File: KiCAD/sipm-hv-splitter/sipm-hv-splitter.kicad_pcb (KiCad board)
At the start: 2 copper layers, 139.7 x 33 mm, 120 parts, among them J1 Conn_02x18_Odd_Even, J2 Conn_02x17_Odd_Even, Q1 BSS138, Q2 BSS138, Q3 BSS138, U1 ATmega328-M, U10 OPA810xDCK, U11 OPA810xDCK, U12 OPA810xDCK, U13 OPA810xDCK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

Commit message: starting placement
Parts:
- added C48: 1.0uF, Capacitor_SMD:C_0603_1608Metric_Pad1.08x0.95mm_HandSolder, F.Cu at (109.0, 92.8)
- added C49: 2.2uF, Capacitor_SMD:C_0603_1608Metric_Pad1.08x0.95mm_HandSolder, F.Cu at (109.0, 95.3)
- added C50: 1.0uF, Capacitor_SMD:C_0603_1608Metric_Pad1.08x0.95mm_HandSolder, F.Cu at (109.0, 97.8)
- added C51: 2.2uF, Capacitor_SMD:C_0603_1608Metric_Pad1.08x0.95mm_HandSolder, F.Cu at (109.0, 100.3)
- added U14: TPS7A25, Package_SON:WSON-6-1EP_2x2mm_P0.65mm_EP1x1.6mm_ThermalVias, F.Cu at (103.3, 94.8)
- added U16: TPS7A25, Package_SON:WSON-6-1EP_2x2mm_P0.65mm_EP1x1.6mm_ThermalVias, F.Cu at (103.3, 98.4)
- C4: value 12nF -> 0.1uF
- C9: value 3.3uF 100V -> 4.7uF 100V
- R13: value R_US -> 150k
- R14: value R_US -> 2.49k
- R6: value 9.76k -> 10k
- moved R37 132.8 mm to (176.5, 55.2)
- moved R29 127.1 mm to (168.7, 53.5), turned to 180 degrees
- moved C40 125.8 mm to (176.5, 57.1)
- moved R21 125.0 mm to (172.7, 57.1), turned to 180 degrees
- moved C32 122.8 mm to (172.7, 55.2), turned to 180 degrees
- moved C16 120.4 mm to (172.7, 53.5)
- moved C24 115.9 mm to (168.6, 58.3)
- moved U6 113.3 mm to (168.6, 55.9)
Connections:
- C16 pad 1: +3.3V -> +3.3VA
- C17 pad 1: +3.3V -> +3.3VA
- C18 pad 1: +3.3V -> +3.3VA
- C19 pad 1: +3.3V -> +3.3VA
- C20 pad 1: +3.3V -> +3.3VA
- C21 pad 1: +3.3V -> +3.3VA
- C22 pad 1: +3.3V -> +3.3VA
- C23 pad 1: +3.3V -> +3.3VA
- J2 pad 10: /-20V -> -24V
- J2 pad 14: /-20V -> -24V
- J2 pad 18: /-20V -> -24V
- J2 pad 2: /-20V -> -24V
- J2 pad 22: /-20V -> -24V
- J2 pad 26: /-20V -> -24V
- J2 pad 30: /-20V -> -24V
- J2 pad 6: /-20V -> -24V
- U10 pad 5: +3.3V -> +3.3VA
- U11 pad 5: +3.3V -> +3.3VA
- U12 pad 5: +3.3V -> +3.3VA
- U13 pad 5: +3.3V -> +3.3VA
- U6 pad 5: +3.3V -> +3.3VA
- U7 pad 5: +3.3V -> +3.3VA
- U8 pad 5: +3.3V -> +3.3VA
- U9 pad 5: +3.3V -> +3.3VA

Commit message: random placement for area estimate
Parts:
- moved R38 95.2 mm to (120.5, 62.8)
- moved R42 94.6 mm to (108.1, 62.7)
- moved R30 90.7 mm to (112.7, 61.0), turned to 180 degrees
- moved R34 90.1 mm to (100.2, 60.9), turned to 180 degrees
- moved C41 87.4 mm to (120.5, 64.7)
- moved R22 87.3 mm to (116.7, 64.7), turned to 180 degrees
- moved R26 86.7 mm to (104.2, 64.6), turned to 180 degrees
- moved C45 86.7 mm to (108.1, 64.6)
- moved C33 84.7 mm to (116.7, 62.8), turned to 180 degrees
- moved C37 84.0 mm to (104.2, 62.7), turned to 180 degrees
- moved R41 82.8 mm to (108.1, 54.9)
- moved C17 82.1 mm to (116.7, 61.0)
- moved C21 81.3 mm to (104.3, 60.9)
- moved R33 80.6 mm to (100.2, 53.1), turned to 180 degrees
- moved C25 77.8 mm to (112.6, 65.9)
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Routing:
- net GND: track 0.00 -> 28.5 mm, vias 0 -> 32
- net -24V: track 0.00 -> 27.7 mm
- net +3.3VA: track 0.00 -> 17.9 mm, vias 0 -> 16
- net Net-(U10--): track 0.00 -> 13.6 mm
- net Net-(U11--): track 0.00 -> 13.6 mm
- net Net-(U12--): track 0.00 -> 13.6 mm
- net Net-(U8--): track 0.00 -> 13.6 mm
- net Net-(U7--): track 0.00 -> 13.6 mm
- net Net-(U13--): track 0.00 -> 13.6 mm
- net Net-(U9--): track 0.00 -> 13.6 mm
- net Net-(U6--): track 0.00 -> 13.6 mm
- net Net-(C38-Pad2): track 0.00 -> 7.83 mm
- net Net-(C35-Pad2): track 0.00 -> 7.83 mm
- net Net-(C32-Pad2): track 0.00 -> 7.83 mm
- net Net-(C33-Pad2): track 0.00 -> 7.83 mm
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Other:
- board size 139.7 x 33 mm -> 82.5 x 33 mm
- copper layers 2 -> 6

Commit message: add ISP
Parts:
- added C52: 1.0uF, Capacitor_SMD:C_0603_1608Metric_Pad1.08x0.95mm_HandSolder, F.Cu at (78.7, 72.4)
- added J3: -OMIT-, Connector_PinHeader_1.00mm:PinHeader_1x06_P1.00mm_Vertical, F.Cu at (91.5, 82.5)
- added R45: 4.7k, Resistor_SMD:R_0603_1608Metric_Pad0.98x0.95mm_HandSolder, F.Cu at (83.8, 82.5)
- C10: footprint Capacitor_SMD:C_0603_1608Metric_Pad1.08x0.95mm_HandSolder -> Capacitor_SMD:C_1206_3216Metric_Pad1.33x1.80mm_HandSolder
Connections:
- C48 pad 2: Net-(U16-GND) -> GND
- C49 pad 2: Net-(U16-GND) -> GND
- C50 pad 2: Net-(U14-GND) -> GND
- C51 pad 2: Net-(U14-GND) -> GND
- U1 pad 18: unconnected-(U1-AVCC-Pad18) -> +3.3V
- U1 pad 21: Net-(U1-GND-Pad21) -> GND
- U1 pad 3: Net-(U1-GND-Pad21) -> GND
- U1 pad 30: unconnected-(U1-PD0-Pad30) -> /COMM/RX
- U1 pad 31: unconnected-(U1-PD1-Pad31) -> /COMM/TX
- U1 pad 33: Net-(U1-GND-Pad21) -> GND
- U1 pad 4: Net-(U1-VCC-Pad4) -> +3.3V
- U1 pad 5: Net-(U1-GND-Pad21) -> GND
- U1 pad 6: Net-(U1-VCC-Pad4) -> +3.3V
- U14 pad 5: Net-(U14-GND) -> GND
- U14 pad 7: Net-(U14-GND) -> GND
- U16 pad 5: Net-(U16-GND) -> GND
- U16 pad 7: Net-(U16-GND) -> GND

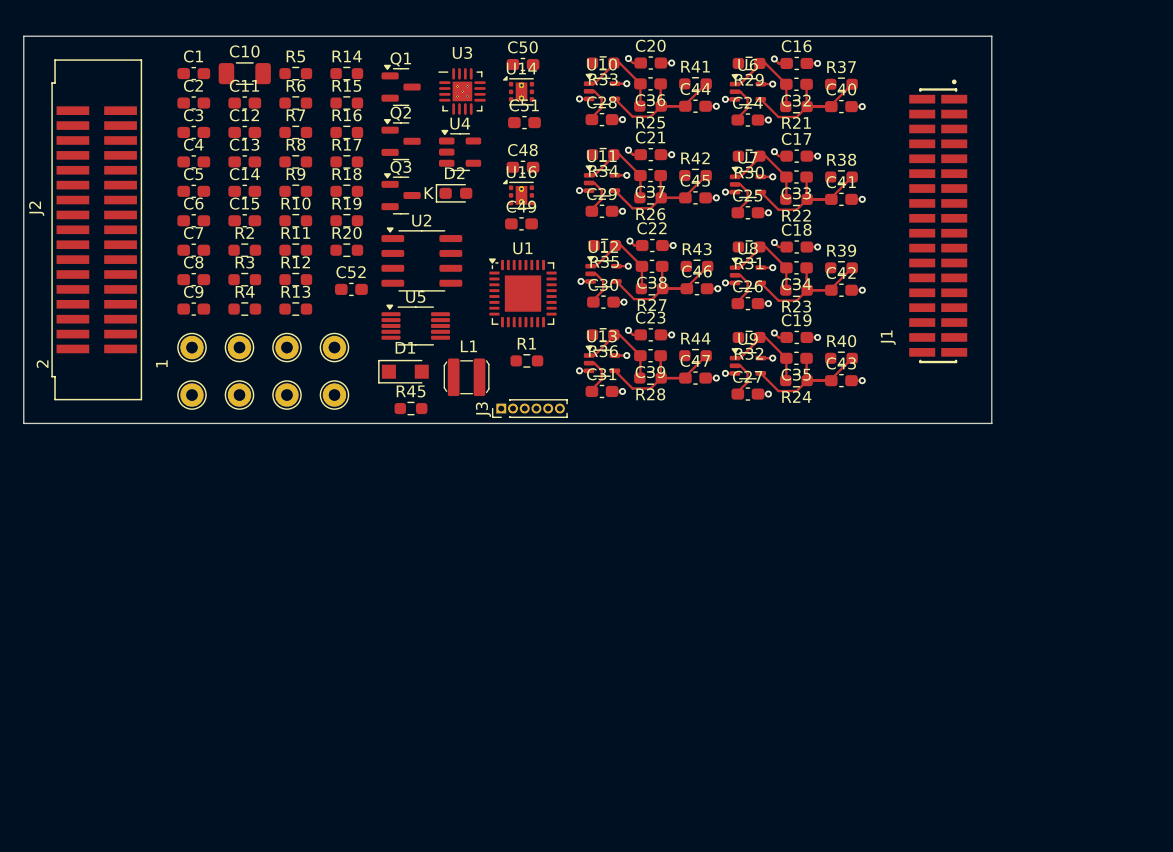
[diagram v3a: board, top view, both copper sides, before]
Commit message: working on 2.5 in placement
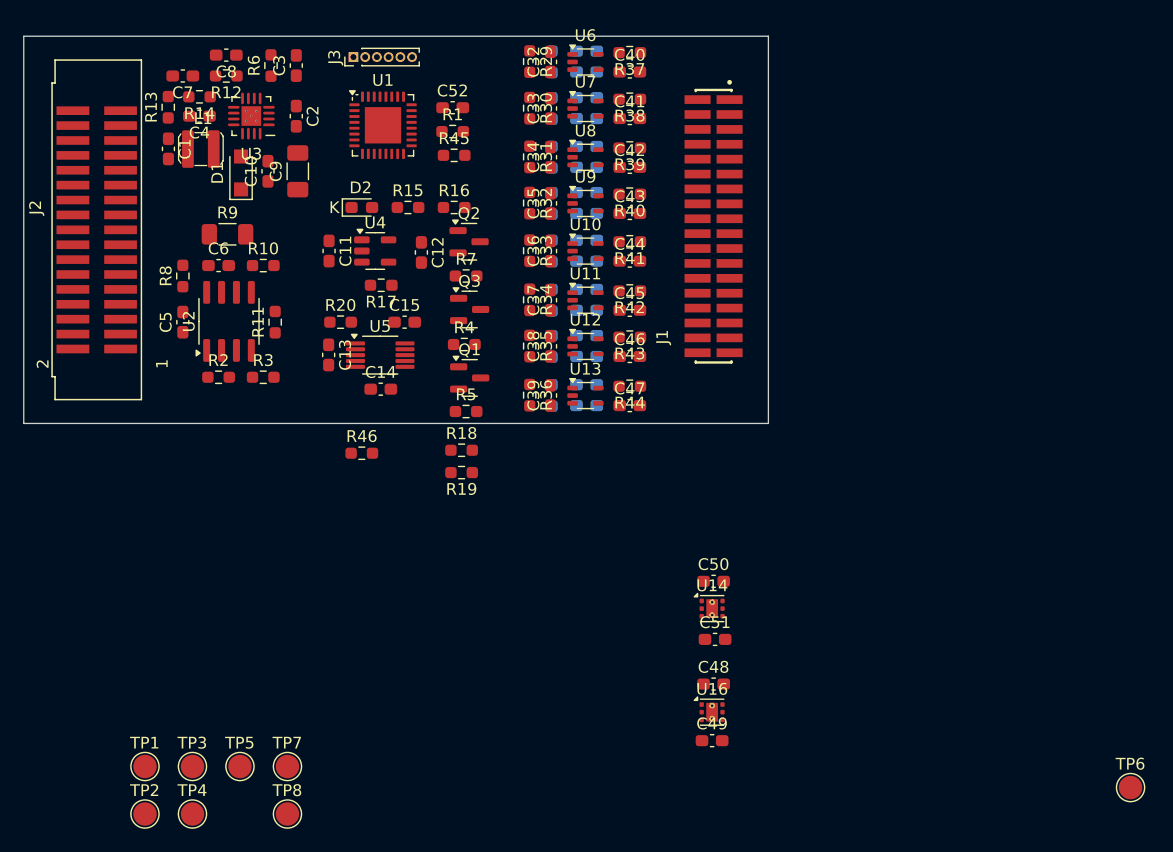
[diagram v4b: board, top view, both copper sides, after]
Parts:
- added R46: 10.0k, Resistor_SMD:R_0603_1608Metric_Pad0.98x0.95mm_HandSolder, F.Cu at (79.6, 86.4)
- C10: footprint Capacitor_SMD:C_1206_3216Metric_Pad1.33x1.80mm_HandSolder -> Capacitor_SMD:C_0603_1608Metric_Pad1.08x0.95mm_HandSolder
- C16, C17, C18, C19, C20, C21, C22, C23, C24, C25, C26, C27, C28, C29, C30, C31, R21, R22, R23, R24, R25, R26, R27, R28: moved to B.Cu
- C9: footprint Capacitor_SMD:C_0603_1608Metric_Pad1.08x0.95mm_HandSolder -> Capacitor_SMD:C_1206_3216Metric_Pad1.33x1.80mm_HandSolder
- R9: footprint Resistor_SMD:R_0603_1608Metric_Pad0.98x0.95mm_HandSolder -> Resistor_SMD:R_1206_3216Metric_Pad1.30x1.75mm_HandSolder
- TP1, TP2, TP3, TP4, TP5, TP6, TP7, TP8: footprint my_tp:tp_SMT_label2 -> TestPoint:TestPoint_Pad_D2.0mm
- moved TP6 79.3 mm to (145.2, 114.9)
- moved C48 47.0 mm to (109.6, 106.0)
- moved U14 47.0 mm to (109.5, 99.6)
- moved U16 47.0 mm to (109.5, 108.4)
- moved C50 47.0 mm to (109.6, 97.3)
- moved C51 47.0 mm to (109.8, 102.2)
- moved C49 47.0 mm to (109.5, 110.9)
- moved TP2 36.0 mm to (61.1, 117.1)
- moved TP4 36.0 mm to (65.2, 117.1)
- moved TP8 36.0 mm to (73.3, 117.1)
- moved TP1 36.0 mm to (61.1, 113.1)
- moved TP3 36.0 mm to (65.2, 113.1)
- moved TP5 36.0 mm to (69.2, 113.1)
- moved TP7 36.0 mm to (73.3, 113.1)
- moved J3 32.5 mm to (78.9, 52.6)
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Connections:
- C3 pad 1: Net-(U3-BIAS) -> +12V
- J1 pad 4: /TEMP -> /THERM
- U1 pad 10: /ADC_IMON -> unconnected-(U1-PD6-Pad10)
- U1 pad 11: /ADC_VMON -> unconnected-(U1-PD7-Pad11)
- U1 pad 23: unconnected-(U1-PC0-Pad23) -> /ADC_IMON
- U1 pad 24: unconnected-(U1-PC1-Pad24) -> /ADC_VMON
- U1 pad 25: unconnected-(U1-PC2-Pad25) -> /THERM
- U3 pad 3: Net-(U3-BIAS) -> +12V
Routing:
- net GND: track 28.5 -> 0.00 mm, vias 32 -> 0
- net -24V: track 27.7 -> 0.00 mm
- net +3.3VA: track 17.9 -> 0.00 mm, vias 16 -> 0
- net Net-(U10--): track 13.6 -> 0.00 mm
- net Net-(U11--): track 13.6 -> 0.00 mm
- net Net-(U12--): track 13.6 -> 0.00 mm
- net Net-(U8--): track 13.6 -> 0.00 mm
- net Net-(U7--): track 13.6 -> 0.00 mm
- net Net-(U13--): track 13.6 -> 0.00 mm
- net Net-(U9--): track 13.6 -> 0.00 mm
- net Net-(U6--): track 13.6 -> 0.00 mm
- net Net-(C38-Pad2): track 7.83 -> 0.00 mm
- net Net-(C35-Pad2): track 7.83 -> 0.00 mm
- net Net-(C32-Pad2): track 7.83 -> 0.00 mm
- net Net-(C33-Pad2): track 7.83 -> 0.00 mm
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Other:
- board size 82.5 x 33 mm -> 63.5 x 33 mm

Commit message: routing madness
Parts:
- added D3: LED, my_smt_led:my_SMT_0603, F.Cu at (85.5, 53.1)
- added R47: 1.5k, Resistor_SMD:R_0603_1608Metric_Pad0.98x0.95mm_HandSolder, F.Cu at (89.4, 53.1)
- TP1, TP2, TP3, TP4, TP5, TP6, TP7, TP8: footprint TestPoint:TestPoint_Pad_D2.0mm -> TestPoint:TestPoint_Pad_D1.0mm
- U1: footprint Package_DFN_QFN:QFN-32-1EP_5x5mm_P0.5mm_EP3.1x3.1mm -> my_QFN:QFN-32-1EP_5x5mm_P0.5mm_EP3.1x3.1mm
- U10, U11, U12, U13, U6, U7, U8, U9: footprint Package_TO_SOT_SMD:Texas_R-PDSO-G5_DCK-5 -> my_SC70:Texas_R-PDSO-G5_DCK-5
- moved TP6 80.4 mm to (77.9, 70.9)
- moved TP7 59.2 mm to (84.6, 55.0)
- moved TP4 51.4 mm to (74.8, 66.7)
- moved TP2 50.6 mm to (65.0, 66.7)
- moved C51 50.2 mm to (63.9, 81.9), turned to 180 degrees
- moved TP8 47.8 mm to (84.8, 70.7)
- moved U14 45.8 mm to (67.3, 81.9)
- moved C49 45.4 mm to (74.5, 81.9), turned to 180 degrees
- moved TP3 42.3 mm to (72.9, 71.5)
- moved TP5 42.1 mm to (81.0, 72.6)
- moved C50 41.8 mm to (70.7, 81.9)
- moved U16 41.3 mm to (77.9, 81.9)
- moved C48 37.1 mm to (81.4, 81.9)
- moved TP1 34.1 mm to (64.8, 79.1)
- moved R46 32.3 mm to (87.5, 55.0)
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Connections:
- net /BOOST/+62V renamed /BOOST/62V
- net Net-(U4-VIN) renamed /BOOST/V62_IN
- J1 pad 1: /DET_0 -> /THERM
- J1 pad 10: /VBIAS -> /DET_5
- J1 pad 12: unconnected-(J1-Pin_12-Pad12) -> /VBIAS
- J1 pad 13: /DET_3 -> unconnected-(J1-Pin_13-Pad13)
- J1 pad 14: /VBIAS -> /DET_4
- J1 pad 16: unconnected-(J1-Pin_16-Pad16) -> /VBIAS
- J1 pad 17: /DET_4 -> unconnected-(J1-Pin_17-Pad17)
- J1 pad 18: /VBIAS -> /DET_3
- J1 pad 2: /VBIAS -> /DET_7
- J1 pad 20: unconnected-(J1-Pin_20-Pad20) -> /VBIAS
- J1 pad 21: /DET_5 -> unconnected-(J1-Pin_21-Pad21)
- J1 pad 22: /VBIAS -> /DET_2
- J1 pad 24: unconnected-(J1-Pin_24-Pad24) -> /VBIAS
- J1 pad 25: /DET_6 -> unconnected-(J1-Pin_25-Pad25)
- J1 pad 26: /VBIAS -> /DET_1
- J1 pad 28: unconnected-(J1-Pin_28-Pad28) -> /VBIAS
- J1 pad 29: /DET_7 -> unconnected-(J1-Pin_29-Pad29)
- J1 pad 30: /VBIAS -> /DET_0
- J1 pad 32: unconnected-(J1-Pin_32-Pad32) -> /VBIAS
- J1 pad 35: GND -> unconnected-(J1-Pin_35-Pad35)
- J1 pad 4: /THERM -> /VBIAS
- J1 pad 5: /DET_1 -> unconnected-(J1-Pin_5-Pad5)
- J1 pad 6: /VBIAS -> /DET_6
- J1 pad 8: unconnected-(J1-Pin_8-Pad8) -> /VBIAS
- J1 pad 9: /DET_2 -> unconnected-(J1-Pin_9-Pad9)
- R29 pad 2: /SIG_0 -> /SIG_7
- R30 pad 2: /SIG_1 -> /SIG_6
- R31 pad 2: /SIG_2 -> /SIG_5
- R32 pad 2: /SIG_3 -> /SIG_4
- R33 pad 2: /SIG_4 -> /SIG_3
- R34 pad 2: /SIG_5 -> /SIG_2
- R35 pad 2: /SIG_6 -> /SIG_1
- R36 pad 2: /SIG_7 -> /SIG_0
- R37 pad 1: /DET_0 -> /DET_7
- R38 pad 1: /DET_1 -> /DET_6
- R39 pad 1: /DET_2 -> /DET_5
- R40 pad 1: /DET_3 -> /DET_4
- R41 pad 1: /DET_4 -> /DET_3
- R42 pad 1: /DET_5 -> /DET_2
- R43 pad 1: /DET_6 -> /DET_1
- R44 pad 1: /DET_7 -> /DET_0
- U1 pad 32: unconnected-(U1-PD2-Pad32) -> Net-(U1-PD2)
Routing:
- net GND: track 0.00 -> 81.5 mm, vias 0 -> 65
- net /SIG_7: track 0.00 -> 45.2 mm, vias 0 -> 2
- net /SIG_6: track 0.00 -> 43.7 mm, vias 0 -> 2
- net /SIG_5: track 0.00 -> 43.4 mm, vias 0 -> 2
- net /SIG_4: track 0.00 -> 42.4 mm, vias 0 -> 2
- net /MISO: track 0.00 -> 36.7 mm, vias 0 -> 2
- net /COMM/RX: track 0.00 -> 30.8 mm, vias 0 -> 2
- net /COMM/TX: track 0.00 -> 26.0 mm, vias 0 -> 2
- net /VR_SHDN: track 0.00 -> 24.8 mm, vias 0 -> 2
- net +12V: track 0.00 -> 24.3 mm, vias 0 -> 19
- net -24V: track 0.00 -> 22.6 mm, vias 0 -> 10
- net +3.3VA: track 0.00 -> 21.1 mm, vias 0 -> 8
- net /~{RESET}: track 0.00 -> 18.7 mm, vias 0 -> 1
- net /BOOST_ENA: track 0.00 -> 18.7 mm, vias 0 -> 2
- net /MOSI: track 0.00 -> 18.7 mm
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- added copper zone on In4.Cu, net +12V
- added copper zone on In4.Cu, net +3.3V
- added copper zone on In3.Cu, net +3.3VA
- added copper zone on In3.Cu, net -24V
- added copper zone on F.Cu, net /BOOST/62V
- added copper zone on F.Cu, net /BOOST/V62_IN
- added copper zone on In4.Cu, net /VBIAS
- added copper zone on In1.Cu, net GND
- added copper zone on F.Cu, net Net-(D1-A)

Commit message: working on bias filter changes
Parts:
- added C53: 1.0uF, Capacitor_SMD:C_0603_1608Metric_Pad1.08x0.95mm_HandSolder, F.Cu at (82.0, 49.1)
- C40, R37: moved to B.Cu
- R21, R22, R23, R24, R25, R26, R27, R28: value 4.7k -> 15k
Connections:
- C32 pad 1: Net-(U6--) -> /DET_7
- C33 pad 1: Net-(U7--) -> /DET_6
- C34 pad 1: Net-(U8--) -> /DET_5
- C35 pad 1: Net-(U9--) -> /DET_4
- C36 pad 1: Net-(U10--) -> /DET_3
- C37 pad 1: Net-(U11--) -> /DET_2
- C38 pad 1: Net-(U12--) -> /DET_1
- C39 pad 1: Net-(U13--) -> /DET_0
- C40 pad 1: Net-(U6--) -> /TIA_0/SIPM_K
- C41 pad 1: Net-(U7--) -> /TIA_1/SIPM_K
- C42 pad 1: Net-(U8--) -> /TIA_2/SIPM_K
- C43 pad 1: Net-(U9--) -> /TIA_3/SIPM_K
- C44 pad 1: Net-(U10--) -> /TIA_4/SIPM_K
- C45 pad 1: Net-(U11--) -> /TIA_5/SIPM_K
- C46 pad 1: Net-(U12--) -> /TIA_6/SIPM_K
- C47 pad 1: Net-(U13--) -> /TIA_7/SIPM_K
- J1 pad 12: /VBIAS -> /TIA_2/SIPM_K
- J1 pad 16: /VBIAS -> /TIA_3/SIPM_K
- J1 pad 20: /VBIAS -> /TIA_4/SIPM_K
- J1 pad 24: /VBIAS -> /TIA_5/SIPM_K
- J1 pad 28: /VBIAS -> unconnected-(J1-Pin_28-Pad28)
- J1 pad 32: /VBIAS -> /TIA_7/SIPM_K
- J1 pad 4: /VBIAS -> /TIA_0/SIPM_K
- J1 pad 8: /VBIAS -> /TIA_1/SIPM_K
- J2 pad 33: /COMM/TX -> /COMM/RX
- J2 pad 34: /COMM/RX -> /COMM/TX
- R1 pad 1: /COMM/TX -> /COMM/RX
- R1 pad 2: /COMM/RX -> /COMM/TX
- R21 pad 1: Net-(U6--) -> /DET_7
- R22 pad 1: Net-(U7--) -> /DET_6
- R23 pad 1: Net-(U8--) -> /DET_5
- R24 pad 1: Net-(U9--) -> /DET_4
- R25 pad 1: Net-(U10--) -> /DET_3
- R26 pad 1: Net-(U11--) -> /DET_2
- R27 pad 1: Net-(U12--) -> /DET_1
- R28 pad 1: Net-(U13--) -> /DET_0
- R37 pad 1: /DET_7 -> /VBIAS
- R37 pad 2: Net-(U6--) -> /TIA_0/SIPM_K
- R38 pad 1: /DET_6 -> /VBIAS
- R38 pad 2: Net-(U7--) -> /TIA_1/SIPM_K
- R39 pad 1: /DET_5 -> /VBIAS
- R39 pad 2: Net-(U8--) -> /TIA_2/SIPM_K
- R40 pad 1: /DET_4 -> /VBIAS
- R40 pad 2: Net-(U9--) -> /TIA_3/SIPM_K
- R41 pad 1: /DET_3 -> /VBIAS
- R41 pad 2: Net-(U10--) -> /TIA_4/SIPM_K
- R42 pad 1: /DET_2 -> /VBIAS
- R42 pad 2: Net-(U11--) -> /TIA_5/SIPM_K
- R43 pad 1: /DET_1 -> /VBIAS
- R43 pad 2: Net-(U12--) -> /TIA_6/SIPM_K
- R44 pad 1: /DET_0 -> /VBIAS
- R44 pad 2: Net-(U13--) -> /TIA_7/SIPM_K
- U10 pad 4: Net-(U10--) -> /DET_3
- U11 pad 4: Net-(U11--) -> /DET_2
- U12 pad 4: Net-(U12--) -> /DET_1
- U13 pad 4: Net-(U13--) -> /DET_0
- U6 pad 4: Net-(U6--) -> /DET_7
- U7 pad 4: Net-(U7--) -> /DET_6
- U8 pad 4: Net-(U8--) -> /DET_5
- U9 pad 4: Net-(U9--) -> /DET_4
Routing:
- net Net-(U11--): track 9.40 -> 0.00 mm, vias 1 -> 0
- net /DET_2: track 0.00 -> 9.40 mm, vias 0 -> 1
- net Net-(U7--): track 9.40 -> 0.00 mm, vias 1 -> 0
- net Net-(U12--): track 9.40 -> 0.00 mm, vias 1 -> 0
- net Net-(U10--): track 9.40 -> 0.00 mm, vias 1 -> 0
- net /DET_3: track 0.00 -> 9.40 mm, vias 0 -> 1
- net /DET_1: track 0.00 -> 9.40 mm, vias 0 -> 1
- net Net-(U9--): track 9.40 -> 0.00 mm, vias 1 -> 0
- net /DET_4: track 0.00 -> 9.40 mm, vias 0 -> 1
- net Net-(U8--): track 9.40 -> 0.00 mm, vias 1 -> 0
- net Net-(U6--): track 9.40 -> 0.00 mm, vias 1 -> 0
- net /DET_5: track 0.00 -> 9.40 mm, vias 0 -> 1
- net Net-(U13--): track 8.77 -> 0.00 mm, vias 1 -> 0
- net /DET_0: track 0.00 -> 8.77 mm, vias 0 -> 1
- net /TIA_0/SIPM_K: track 0.00 -> 5.06 mm, vias 0 -> 1
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
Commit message: routing
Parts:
- C41, C42, C43, C44, C45, C46, C47, R38, R39, R40, R41, R42, R43, R44: moved to B.Cu
- moved C53 13.4 mm to (88.6, 60.8)
- moved R1 11.6 mm to (77.1, 53.8), turned to -90 degrees
- moved R46 4.22 mm to (88.6, 59.1)
- moved R45 3.86 mm to (88.6, 57.3)
- moved C8 3.37 mm to (71.0, 54.1)
- moved D3 3.20 mm to (88.6, 53.5), turned to 180 degrees
- moved J3 2.92 mm to (79.9, 53.2)
- moved R47 2.53 mm to (88.6, 55.5), turned to 0 degrees
- moved R6 1.74 mm to (73.5, 53.8)
- moved TP7 1.45 mm to (86.0, 55.4)
- moved C3 1.38 mm to (75.3, 53.8)
- moved R16 1.31 mm to (88.6, 63.6)
- moved C24 0.97 mm to (98.8, 54.8)
- moved C40 0.97 mm to (102.5, 54.8)
- moved C16 0.97 mm to (98.8, 53.0)
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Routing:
- net /SIG_7: track 45.2 -> 0.00 mm, vias 2 -> 0
- net /ADC_IMON: track 5.19 -> 49.8 mm, vias 0 -> 2
- net /SIG_6: track 43.7 -> 0.00 mm, vias 2 -> 0
- net /SIG_5: track 43.4 -> 0.00 mm, vias 2 -> 0
- net GND: track 81.6 -> 38.6 mm, vias 65 -> 26
- net /SIG_4: track 42.4 -> 0.00 mm, vias 2 -> 0
- net Net-(Q2-G): track 0.00 -> 38.9 mm, vias 0 -> 4
- net Net-(Q1-D): track 0.00 -> 28.3 mm, vias 0 -> 2
- net /SCK: track 0.00 -> 27.0 mm, vias 0 -> 2
- net +12V: track 24.3 -> 0.00 mm, vias 19 -> 0
- net /VR_RESET: track 2.08 -> 26.2 mm, vias 0 -> 2
- net /BOOST/SHDN: track 11.2 -> 30.2 mm, vias 0 -> 2
- net +3.3V: track 18.6 -> 0.00 mm, vias 12 -> 0
- net /ADC_VMON: track 0.00 -> 17.3 mm, vias 0 -> 2
- net /~{SYNC}: track 0.00 -> 17.2 mm, vias 0 -> 2
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
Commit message: routing almost done
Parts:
- moved C14 0.24 mm to (81.7, 78.4)
- turned R20 to 180 degrees
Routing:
- net GND: track 38.6 -> 91.9 mm, vias 26 -> 69
- net /THERM: track 10.1 -> 39.9 mm, vias 2 -> 3
- net +3.3V: track 0.00 -> 15.1 mm, vias 0 -> 15
- net /TIA_7/SIPM_K: track 5.06 -> 14.8 mm
- net +12V: track 0.00 -> 9.34 mm, vias 0 -> 10
- net /DET_0: track 10.8 -> 19.8 mm
- net /BOOST/62V: track 0.00 -> 6.75 mm
- net Net-(U3-FB): track 0.00 -> 6.55 mm
- net Net-(U2-V_{IN+}): track 0.00 -> 4.58 mm
- net Net-(U5-A): track 2.57 -> 5.97 mm
- net /BOOST/SHDN: track 30.2 -> 33.3 mm, vias 2 -> 5
- net Net-(U4-ADJ): track 11.2 -> 8.67 mm
- net Net-(U5-EXT_CAP): track 0.00 -> 2.54 mm
- net Net-(Q2-G): track 38.9 -> 40.9 mm
- net /PGOOD: track 10.7 -> 12.2 mm
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- added copper zone on F.Cu, net /VBIAS
